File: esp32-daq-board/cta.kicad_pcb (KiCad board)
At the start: 2 copper layers, 198.1 x 99.1 mm, 38 parts, among them J1 Barrel_Jack_MountingPin, J2 Conn_01x15_Female, J3 Conn_01x15_Female, J5V1 Conn_01x03, U5V1 LM7805_TO220

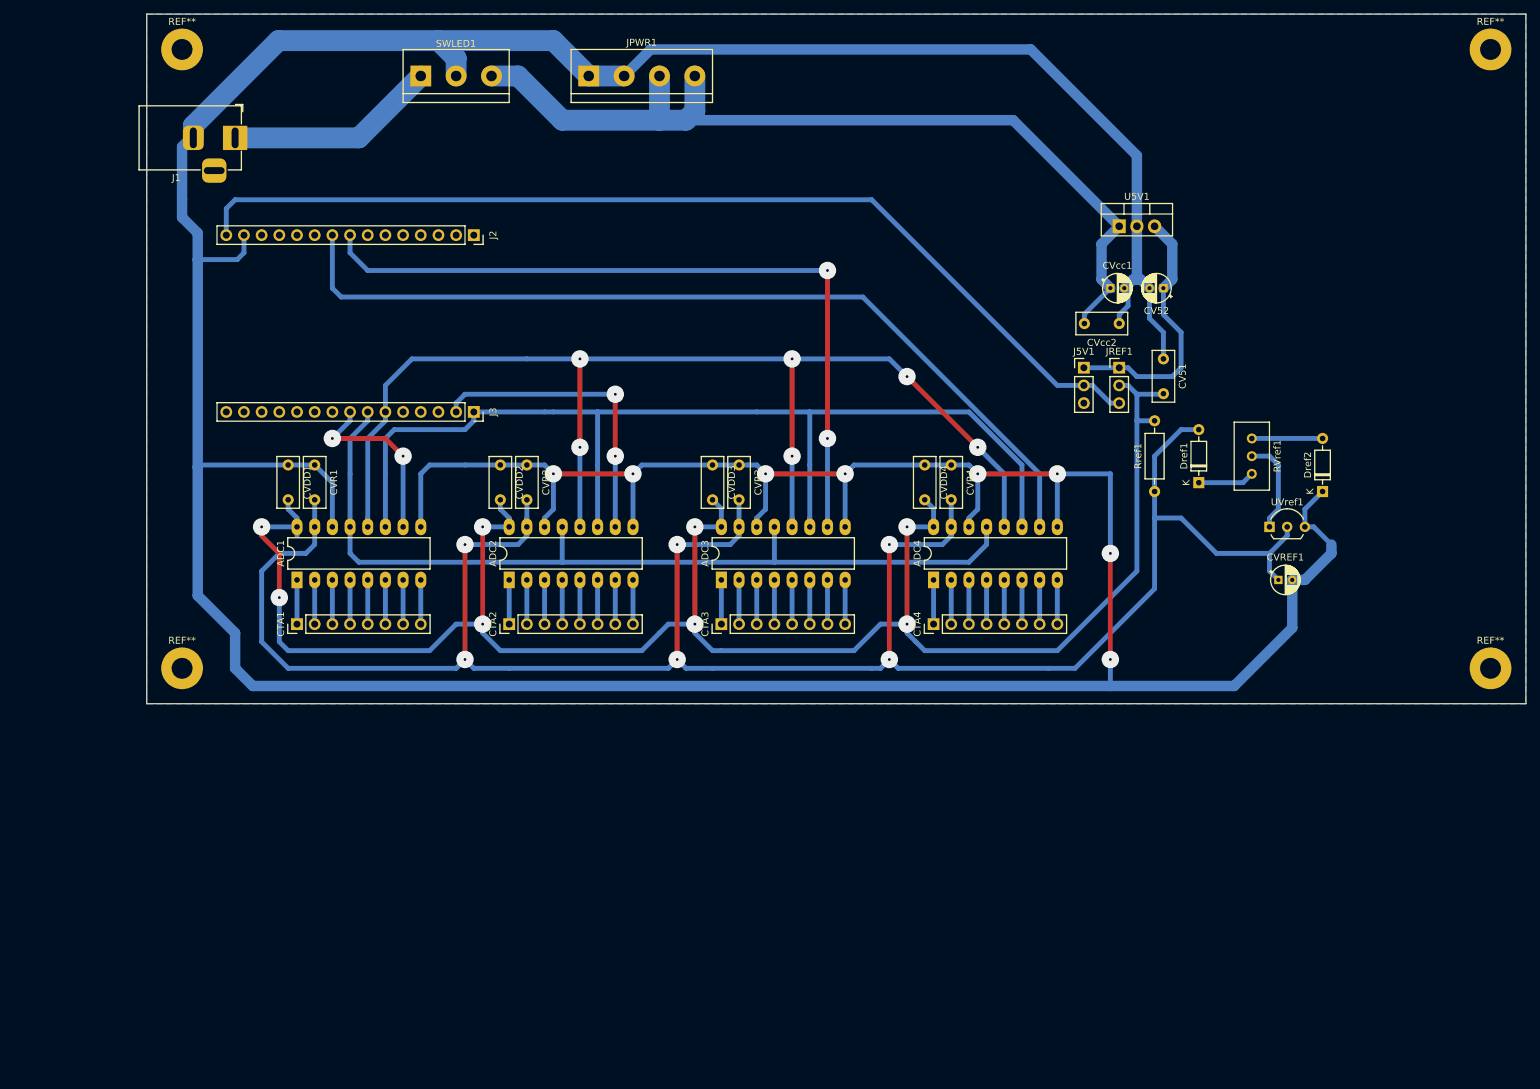
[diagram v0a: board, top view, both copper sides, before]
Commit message: Major changes in the esp daq board.
Now the analog ground is given in a ninth wire for each board in the same flat cable.

Power supply will be from the ESP board.
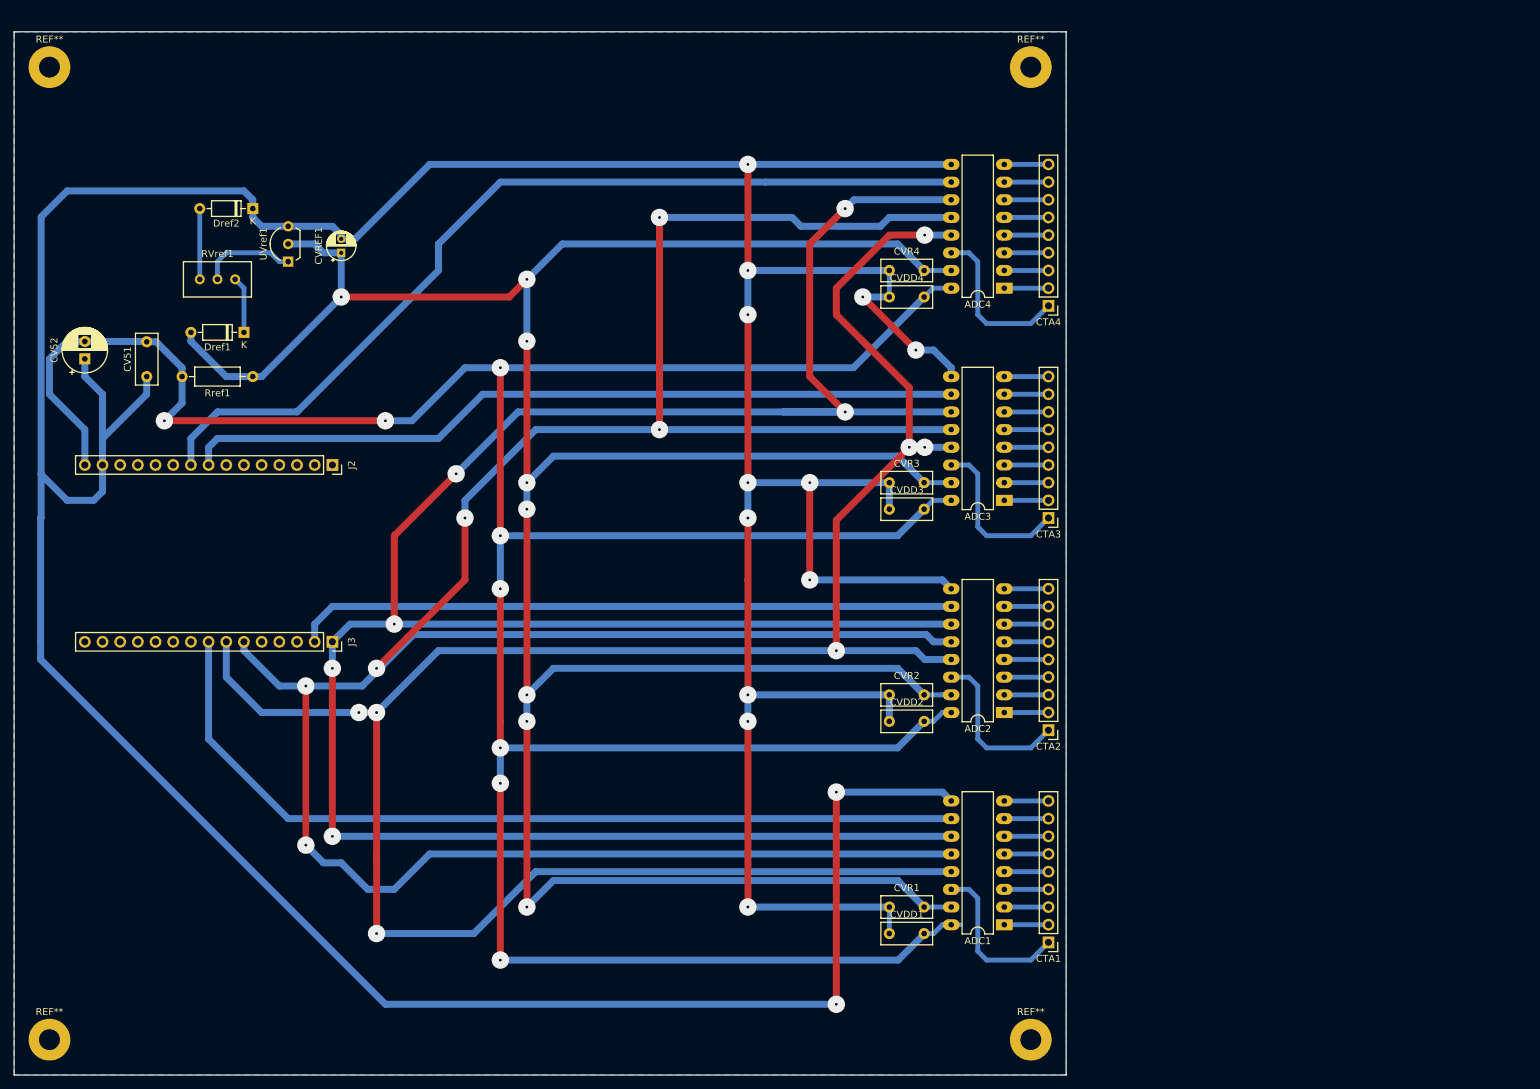
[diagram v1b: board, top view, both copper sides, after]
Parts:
- removed CVcc1: 10u, Capacitor_THT:CP_Radial_D4.0mm_P2.00mm
- removed CVcc2: 100n, Capacitor_THT:C_Rect_L7.2mm_W3.0mm_P5.00mm_FKS2_FKP2_MKS2_MKP2
- removed J1: Barrel_Jack_MountingPin, Connector_BarrelJack:BarrelJack_Horizontal
- removed J5V1, JREF1: Conn_01x03, Connector_PinHeader_2.54mm:PinHeader_1x03_P2.54mm_Vertical
- removed JPWR1: Conn_01x04, TerminalBlock:TerminalBlock_bornier-4_P5.08mm
- removed the REF** at (231.1, 43.2)
- removed the REF** at (231.1, 132.1)
- removed the REF** at (43.2, 132.1)
- removed the REF** at (43.2, 43.2)
- removed SWLED1: Conn_01x03, TerminalBlock:TerminalBlock_bornier-3_P5.08mm
- removed U5V1: LM7805_TO220, Package_TO_SOT_THT:TO-220-3_Vertical
- added REF**: MountingHole_3mm_Pad, MountingHole:MountingHole_3mm_Pad, F.Cu at (165.1, 185.4)
- added REF**: MountingHole_3mm_Pad, MountingHole:MountingHole_3mm_Pad, F.Cu at (24.1, 185.4)
- added REF**: MountingHole_3mm_Pad, MountingHole:MountingHole_3mm_Pad, F.Cu at (24.1, 45.7)
- added REF**: MountingHole_3mm_Pad, MountingHole:MountingHole_3mm_Pad, F.Cu at (165.1, 45.7)
- CTA1, CTA2, CTA3, CTA4: value Conn_01x08 -> Conn_01x09; footprint Connector_PinHeader_2.54mm:PinHeader_1x08_P2.54mm_Vertical -> Connector_PinHeader_2.54mm:PinHeader_1x09_P2.54mm_Vertical
- CV52: value 10u -> 100u; footprint Capacitor_THT:CP_Radial_D4.0mm_P2.00mm -> Capacitor_THT:CP_Radial_D6.3mm_P2.50mm
- CVREF1: value 10u -> 1u
- moved Dref2 159.0 mm to (53.3, 66.0), turned to 180 degrees
- moved CV52 155.3 mm to (29.2, 87.6), turned to 90 degrees
- moved RVref1 148.7 mm to (50.8, 76.2), turned to 0 degrees
- moved CV51 146.1 mm to (38.1, 90.2), turned to 90 degrees
- moved UVref1 146.0 mm to (58.4, 73.7), turned to 90 degrees
- moved CVREF1 142.6 mm to (66.0, 72.4), turned to 90 degrees
- moved Dref1 138.8 mm to (52.1, 83.8), turned to 180 degrees
- moved Rref1 130.6 mm to (53.3, 90.2), turned to 180 degrees
- moved CTA1 117.2 mm to (167.6, 171.4), turned to 180 degrees
- moved ADC1 113.0 mm to (161.3, 168.9), turned to 180 degrees
- moved CVDD1 109.5 mm to (144.8, 170.2), turned to 0 degrees
- moved CVR1 104.1 mm to (144.8, 166.4), turned to 0 degrees
- moved CTA2 79.0 mm to (167.6, 141.0), turned to 180 degrees
- moved ADC2 73.6 mm to (161.3, 138.4), turned to 180 degrees
- moved CVDD2 66.9 mm to (144.8, 139.7), turned to 0 degrees
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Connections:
- ADC1 pad 14: GND -> /AGND1
- ADC2 pad 14: GND -> /AGND2
- ADC3 pad 14: GND -> /AGND3
- ADC4 pad 14: GND -> /AGND4
- CTA1 pad 1: Net-(ADC1-Pad1) -> /AGND1
- CTA1 pad 2: Net-(ADC1-Pad2) -> Net-(ADC1-Pad1)
- CTA1 pad 3: Net-(ADC1-Pad3) -> Net-(ADC1-Pad2)
- CTA1 pad 4: Net-(ADC1-Pad4) -> Net-(ADC1-Pad3)
- CTA1 pad 5: Net-(ADC1-Pad5) -> Net-(ADC1-Pad4)
- CTA1 pad 6: Net-(ADC1-Pad6) -> Net-(ADC1-Pad5)
- CTA1 pad 7: Net-(ADC1-Pad7) -> Net-(ADC1-Pad6)
- CTA1 pad 8: Net-(ADC1-Pad8) -> Net-(ADC1-Pad7)
- CTA2 pad 1: Net-(ADC2-Pad1) -> /AGND2
- CTA2 pad 2: Net-(ADC2-Pad2) -> Net-(ADC2-Pad1)
- CTA2 pad 3: Net-(ADC2-Pad3) -> Net-(ADC2-Pad2)
- CTA2 pad 4: Net-(ADC2-Pad4) -> Net-(ADC2-Pad3)
- CTA2 pad 5: Net-(ADC2-Pad5) -> Net-(ADC2-Pad4)
- CTA2 pad 6: Net-(ADC2-Pad6) -> Net-(ADC2-Pad5)
- CTA2 pad 7: Net-(ADC2-Pad7) -> Net-(ADC2-Pad6)
- CTA2 pad 8: Net-(ADC2-Pad8) -> Net-(ADC2-Pad7)
- CTA3 pad 1: Net-(ADC3-Pad1) -> /AGND3
- CTA3 pad 2: Net-(ADC3-Pad2) -> Net-(ADC3-Pad1)
- CTA3 pad 3: Net-(ADC3-Pad3) -> Net-(ADC3-Pad2)
- CTA3 pad 4: Net-(ADC3-Pad4) -> Net-(ADC3-Pad3)
- CTA3 pad 5: Net-(ADC3-Pad5) -> Net-(ADC3-Pad4)
- CTA3 pad 6: Net-(ADC3-Pad6) -> Net-(ADC3-Pad5)
- CTA3 pad 7: Net-(ADC3-Pad7) -> Net-(ADC3-Pad6)
- CTA3 pad 8: Net-(ADC3-Pad8) -> Net-(ADC3-Pad7)
- CTA4 pad 1: Net-(ADC4-Pad1) -> /AGND4
- CTA4 pad 2: Net-(ADC4-Pad2) -> Net-(ADC4-Pad1)
- CTA4 pad 3: Net-(ADC4-Pad3) -> Net-(ADC4-Pad2)
- CTA4 pad 4: Net-(ADC4-Pad4) -> Net-(ADC4-Pad3)
- CTA4 pad 5: Net-(ADC4-Pad5) -> Net-(ADC4-Pad4)
- CTA4 pad 6: Net-(ADC4-Pad6) -> Net-(ADC4-Pad5)
- CTA4 pad 7: Net-(ADC4-Pad7) -> Net-(ADC4-Pad6)
- CTA4 pad 8: Net-(ADC4-Pad8) -> Net-(ADC4-Pad7)
- CV52 pad 1: /V5V -> GND
- CV52 pad 2: GND -> /VDD
- J2 pad 15: /VIN -> /VDD
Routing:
- net /MISO: track 175.8 -> 407.3 mm
- net /MOSI: track 154.1 -> 367.5 mm, vias 0 -> 6
- net /CLK: track 127.1 -> 323.0 mm, vias 0 -> 7
- net /VDD: track 269.9 -> 455.6 mm
- net /VIN: track 144.7 -> 0.00 mm
- net VCC: track 129.4 -> 0.00 mm
- net /Vref: track 311.6 -> 419.1 mm, vias 6 -> 8
- net /CS1: track 26.2 -> 125.4 mm, vias 2 -> 0
- net /CS2: track 43.7 -> 95.0 mm, vias 2 -> 0
- net /V5V: track 38.0 -> 0.00 mm
- net /VCCIN: track 30.4 -> 0.00 mm
- net /AGND1: track 0.00 -> 23.7 mm
- net /AGND3: track 0.00 -> 23.7 mm
- net /AGND4: track 0.00 -> 23.7 mm
- net /AGND2: track 0.00 -> 23.7 mm
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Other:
- board size 198.1 x 99.1 mm -> 151.1 x 149.9 mm

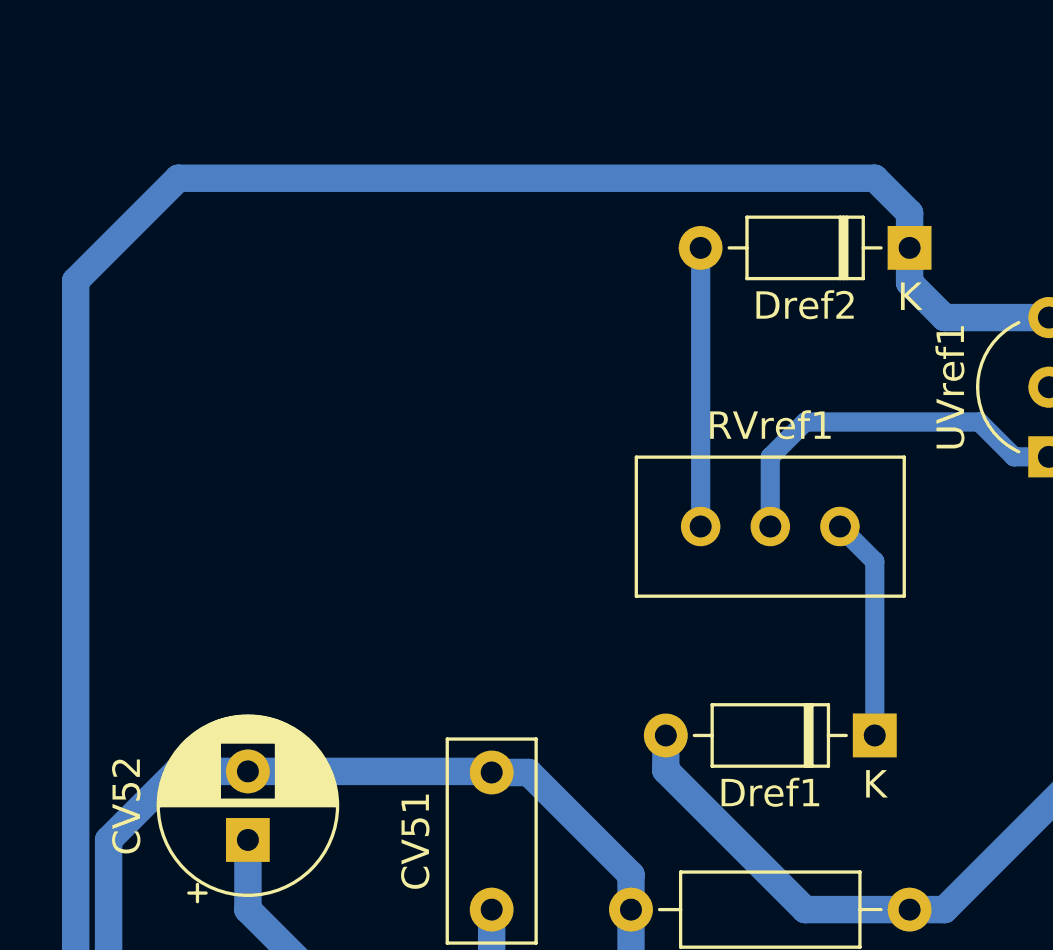
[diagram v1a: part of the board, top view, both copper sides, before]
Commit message: Added a terminal block to esp32-daq-board
This terminal exposes the 5V supply, reference voltage and ground. This makes it easier to adjust the the reference voltage.
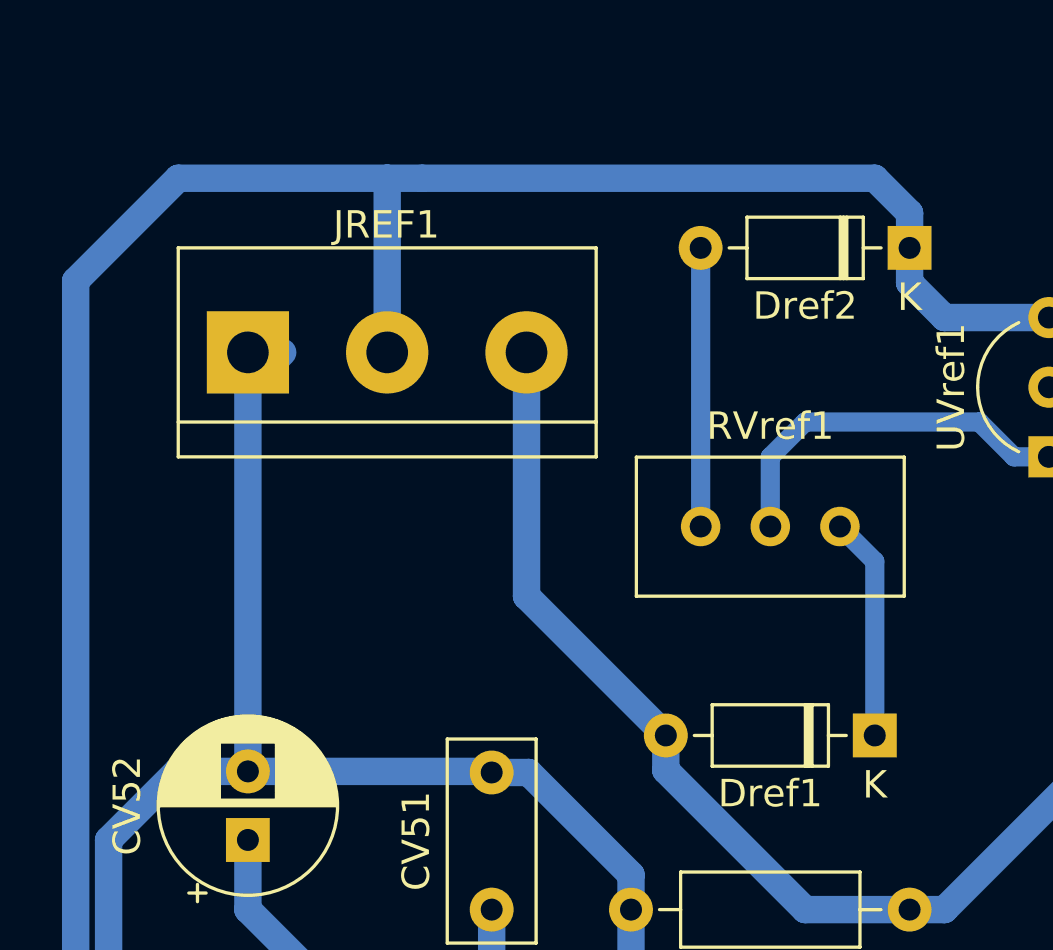
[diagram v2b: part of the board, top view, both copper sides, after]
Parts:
- added JREF1: Conn_01x03, TerminalBlock:TerminalBlock_bornier-3_P5.08mm, F.Cu at (29.2, 69.8)
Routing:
- net /VDD: track 455.6 -> 472.7 mm
- net /Vref: track 419.1 -> 435.2 mm
- net GND: track 689.8 -> 696.2 mm

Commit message: Unifying all the grounds AGND and DGND
On the previous version, each anemometer had a ground that was connected to the AGND present in the MCP3208. This was burning the MCP3208. I still need to undersant how to work with this AGND properly.
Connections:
- ADC1 pad 14: /AGND1 -> GND
- ADC2 pad 14: /AGND2 -> GND
- ADC3 pad 14: /AGND3 -> GND
- ADC4 pad 14: /AGND4 -> GND
- CTA1 pad 1: /AGND1 -> GND
- CTA2 pad 1: /AGND2 -> GND
- CTA3 pad 1: /AGND3 -> GND
- CTA4 pad 1: /AGND4 -> GND
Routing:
- net GND: track 696.2 -> 791.0 mm
- net /AGND1: track 23.7 -> 0.00 mm
- net /AGND3: track 23.7 -> 0.00 mm
- net /AGND4: track 23.7 -> 0.00 mm
- net /AGND2: track 23.7 -> 0.00 mm
